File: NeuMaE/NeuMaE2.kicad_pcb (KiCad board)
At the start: 2 copper layers, 40.4 x 50 mm, 22 parts, among them J1 MOTOR, J2 PROGRAM, J3 LED, J4 PWR, J5 EXTRA, J6 PWR, Q1 BC337, SW1 FLASH, SW2 RESET, U1 PMIC-LD1117V33(TO-220)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

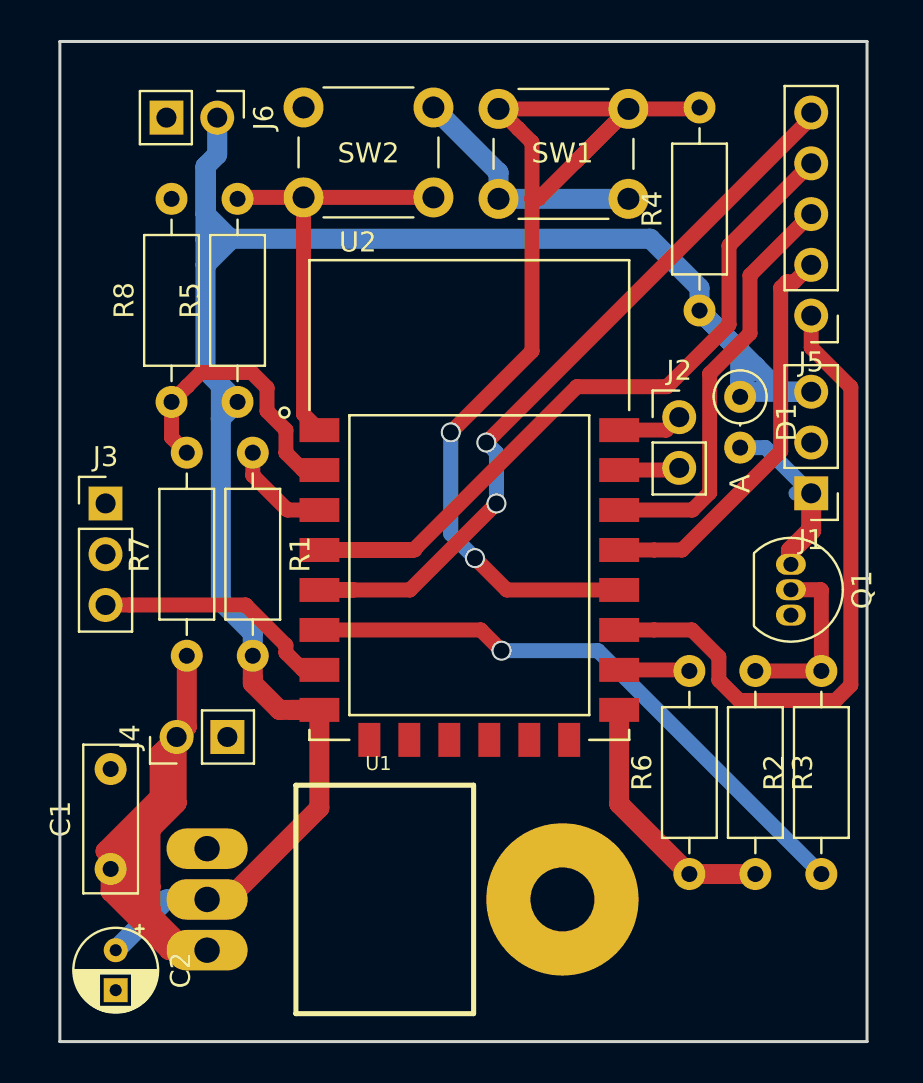
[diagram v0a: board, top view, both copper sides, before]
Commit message: made even smaller pcb by putting voltage regulator on other side
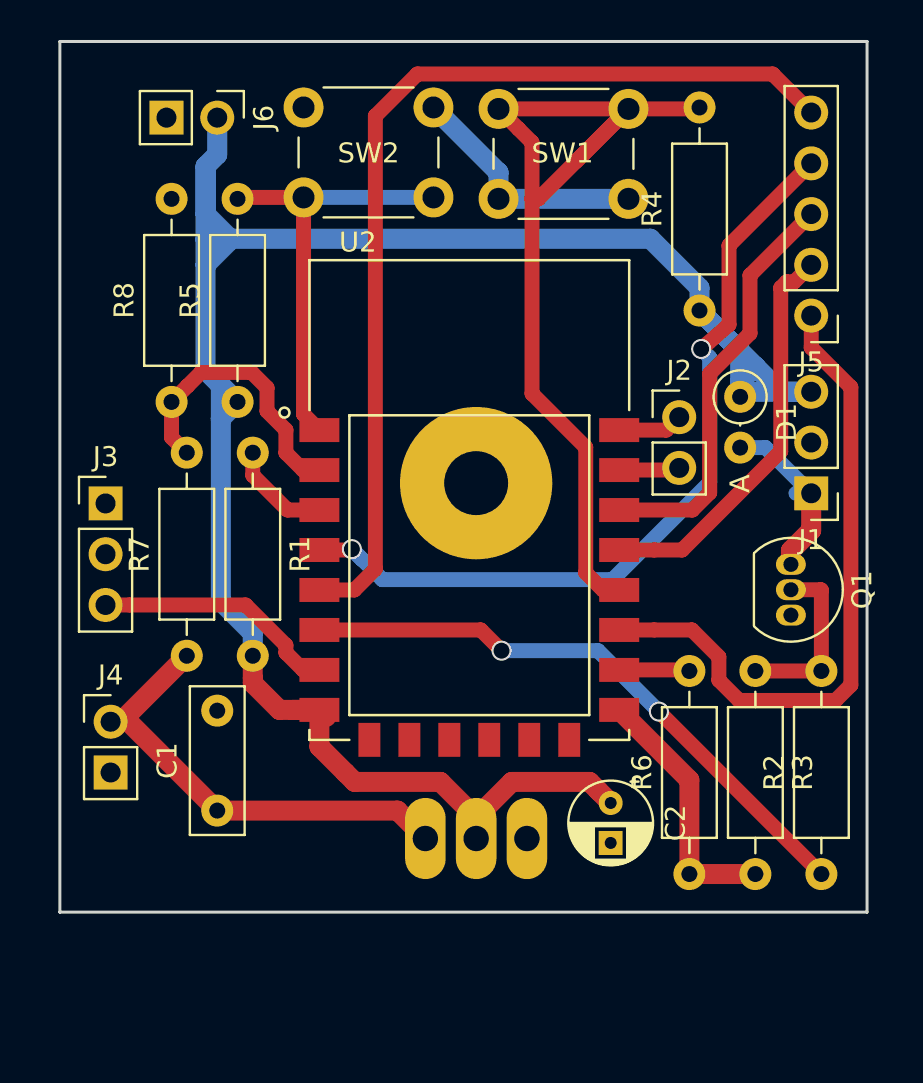
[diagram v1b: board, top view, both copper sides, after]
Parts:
- U1: moved to B.Cu
- moved C2 25.8 mm to (75.3, 52.8)
- moved U1 14.6 mm to (68.6, 43.2), turned to 180 degrees
- moved C1 6.08 mm to (55.6, 53.2)
- moved J4 3.39 mm to (50.3, 48.8), turned to 0 degrees
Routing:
- net VCC: track 47.8 -> 23.3 mm
- net /PIN5: track 38.9 -> 49.6 mm, vias 2 -> 0
- net Net-(R4-Pad2): track 54.2 -> 48.0 mm, vias 2 -> 0
- net Net-(U1-PadHEAT): track 0.00 -> 3.26 mm
- net +3V3: track 107.1 -> 110.0 mm
- net /PIN4: track 40.3 -> 42.0 mm, vias 0 -> 2
- net GND: track 28.1 -> 27.6 mm
- net /MOTOR: vias 1 -> 2
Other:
- board size 40.4 x 50 mm -> 40.4 x 43.6 mm
